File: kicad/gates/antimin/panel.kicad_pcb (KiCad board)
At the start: 2 copper layers, 100 x 100 mm, 1201 parts, among them J1 Conn_01x03, J2 Conn_01x03, Q1 BSS8402DW-7-F, Q2 BSS8402DW-7-F

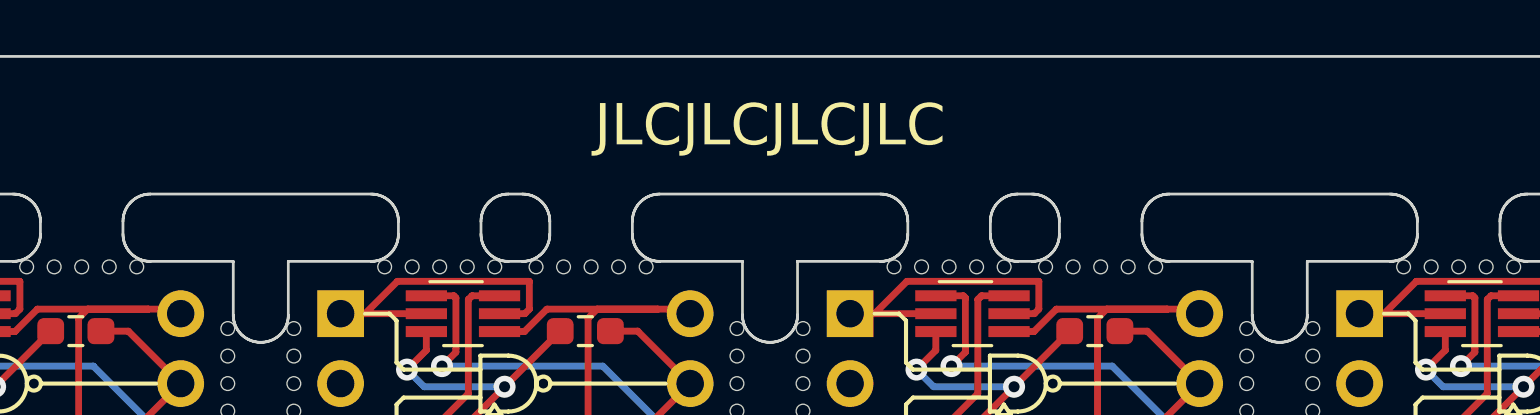
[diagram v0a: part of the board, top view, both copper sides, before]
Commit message: fixed sum logic gate schematic and simulation
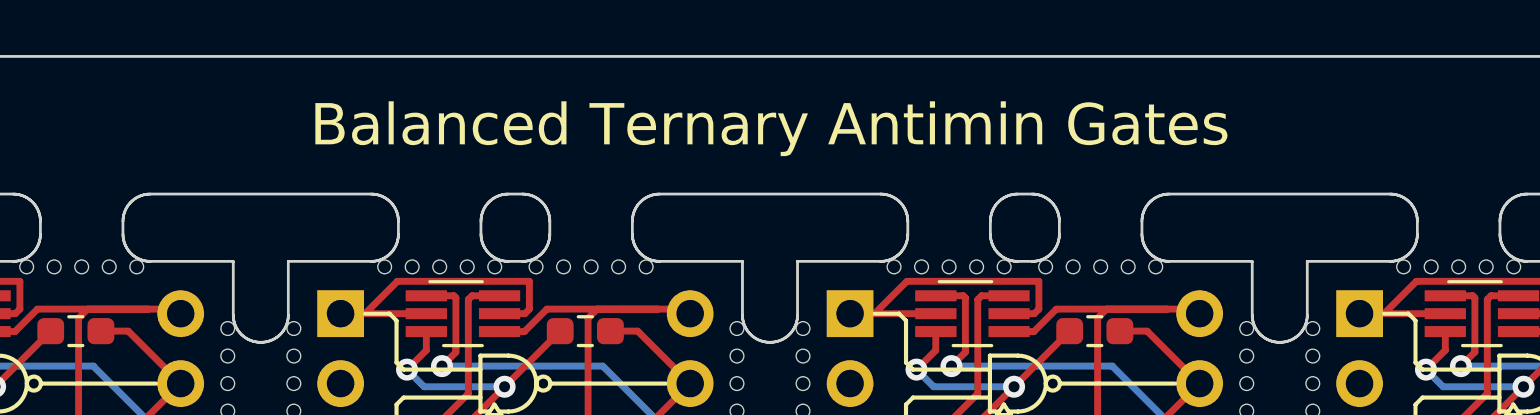
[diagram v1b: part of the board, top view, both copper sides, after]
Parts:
- removed the REF** at (110.0, 17.5) (x2)
- removed the REF** at (20.0, 17.5) (x2)
- removed the REF** at (20.0, 112.5) (x2)
- added REF**: Fiducial, Fiducial, B.Cu at (110.0, 17.5)
- added REF**: Fiducial, Fiducial, B.Cu at (20.0, 17.5)
- added REF**: Fiducial, Fiducial, B.Cu at (20.0, 112.5)
- added REF**: Fiducial, Fiducial, F.Cu at (110.0, 17.5)
- added REF**: Fiducial, Fiducial, F.Cu at (20.0, 112.5)
- added REF**: Fiducial, Fiducial, F.Cu at (20.0, 17.5)
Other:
- board text added: "Balanced Ternary Antimin Gates"
- board text removed: "JLCJLCJLCJLC"
